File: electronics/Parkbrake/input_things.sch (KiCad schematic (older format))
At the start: 14 parts, among them Q31 BSS138, U27 SN74LVC245ADBR

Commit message: traceroute finished although there probably is some errors
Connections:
- net IGN_ON_SIG: now also U27.9 (O0b); no longer U27.7 (O1b)
- net IGN_ON_SIGNAL: now also U27.11 (I0b); no longer U27.13 (I1b)
- net RELEASE_CMD_SIG: now also U27.7 (O1b); no longer U27.9 (O0b)
- net SAFE_TO_RELEASE: now also U27.13 (I1b); no longer U27.11 (I0b)
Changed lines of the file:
@@
 Text GLabel 7500 2475 0    60   Input ~ 0
 BRAKELIGHTS_ON_SIGNAL
-Text GLabel 7500 2850 0    60   Input ~ 0
+Text GLabel 7500 2725 0    60   Input ~ 0
 IGN_ON_SIGNAL
 Text GLabel 7500 2225 0    60   Input ~ 0
@@
 Text GLabel 7500 2975 0    60   Input ~ 0
 TIGHTEN_CMD
-Text GLabel 7500 2725 0    60   Input ~ 0
+Text GLabel 7500 2850 0    60   Input ~ 0
 SAFE_TO_RELEASE
 Text GLabel 7500 2600 0    60   Input ~ 0
@@
 $EndComp
 $Comp
-L GND #PWR093
+L GND #PWR092
 U 1 1 5793D9FE
 P 8400 2000
-F 0 "#PWR093" H 8400 1750 50  0001 C CNN
+F 0 "#PWR092" H 8400 1750 50  0001 C CNN
 F 1 "GND" H 8400 1850 50  0001 C CNN
 F 2 "" H 8400 2000 50  0000 C CNN
@@
 +12V_powerFront
 $Comp
-L GND #PWR094
+L GND #PWR093
 U 1 1 5793F3F6
 P 2625 3025
-F 0 "#PWR094" H 2625 2775 50  0001 C CNN
+F 0 "#PWR093" H 2625 2775 50  0001 C CNN
 F 1 "GND" H 2625 2875 50  0000 C CNN
 F 2 "" H 2625 3025 50  0000 C CNN
@@
 Text GLabel 9200 2600 2    60   Input ~ 0
 PWR_ENABLED_SIG
+Text GLabel 9200 2850 2    60   Input ~ 0
+RELEASE_CMD_SIG
 Text GLabel 9200 2725 2    60   Input ~ 0
-RELEASE_CMD_SIG
-Text GLabel 9200 2850 2    60   Input ~ 0
 IGN_ON_SIG
 Text GLabel 9200 2975 2    60   Input ~ 0
@@
 +12V_feed
 $Comp
-L GND #PWR095
+L GND #PWR094
 U 1 1 57945BF9
 P 2600 5425
-F 0 "#PWR095" H 2600 5175 50  0001 C CNN
+F 0 "#PWR094" H 2600 5175 50  0001 C CNN
 F 1 "GND" H 2600 5275 50  0000 C CNN
 F 2 "" H 2600 5425 50  0000 C CNN
@@
 $EndComp
 $Comp
-L GND #PWR096
+L GND #PWR095
 U 1 1 57942417
 P 7725 5375
-F 0 "#PWR096" H 7725 5125 50  0001 C CNN
+F 0 "#PWR095" H 7725 5125 50  0001 C CNN
 F 1 "GND" H 7725 5225 50  0000 C CNN
 F 2 "" H 7725 5375 50  0000 C CNN

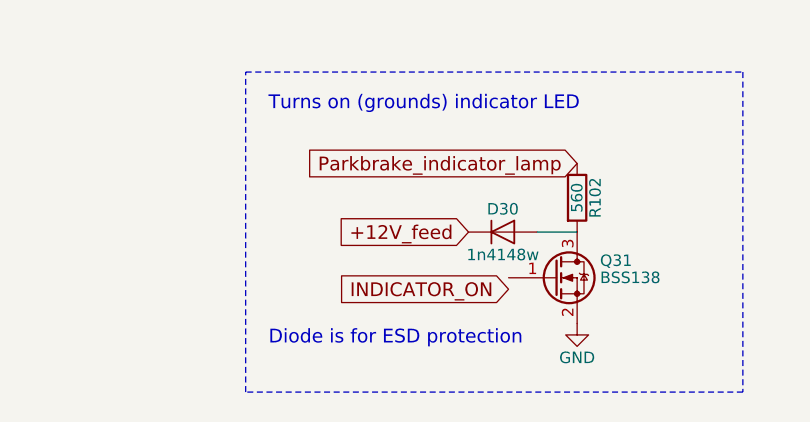
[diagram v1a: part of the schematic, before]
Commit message: minor tweaks to pcb, had a cap on wrong polarity
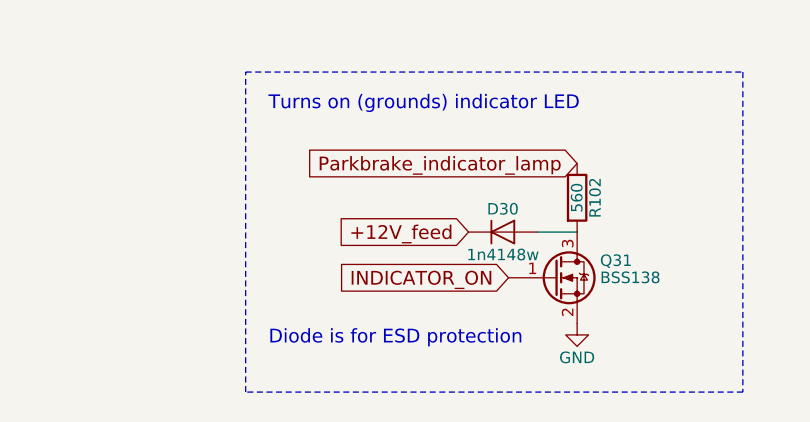
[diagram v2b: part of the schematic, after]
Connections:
- net INDICATOR_ON: now also Q31.1 (G)
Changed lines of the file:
@@
 U 1 1 57942372
 P 7625 5175
+AR Path="/57942372" Ref="Q31"  Part="1"
+AR Path="/570A3FC3/5793D1EA/57942372" Ref="Q31"  Part="1"
 F 0 "Q31" H 7825 5250 50  0000 L CNN
 F 1 "BSS138" H 7825 5175 50  0000 L CNN
@@
 Text GLabel 7725 4675 0    60   Input ~ 0
 Parkbrake_indicator_lamp
-Text GLabel 7425 5225 0    60   Input ~ 0
+Text GLabel 7425 5175 0    60   Input ~ 0
 INDICATOR_ON
 Text Notes 6375 4450 0    60   ~ 0
